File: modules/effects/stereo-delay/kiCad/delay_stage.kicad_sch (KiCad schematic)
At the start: 23 parts, among them Q2 2N3904, U6 PT2399

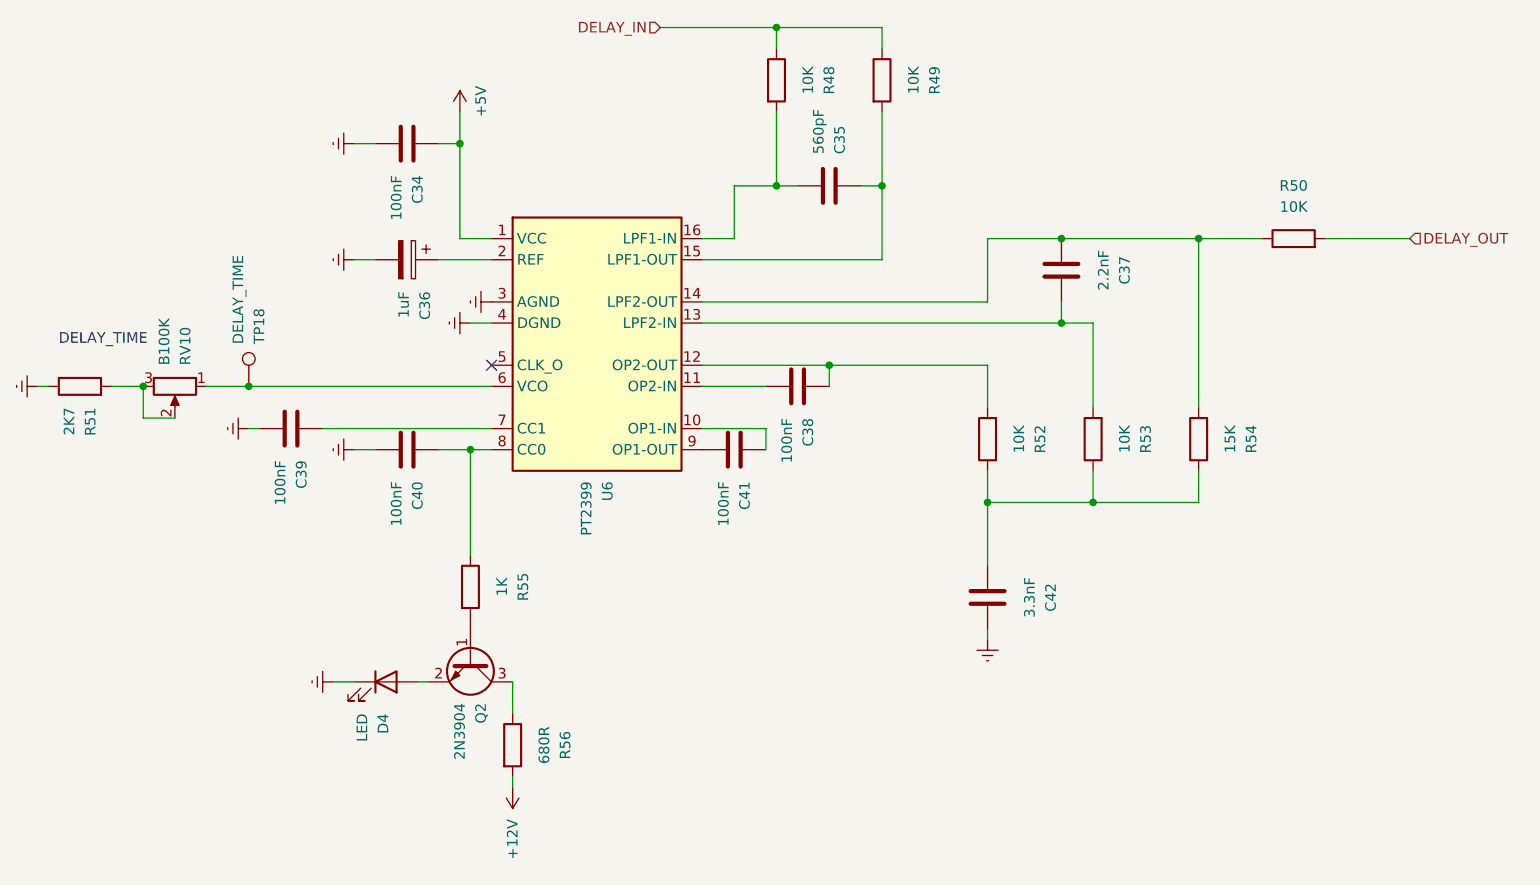
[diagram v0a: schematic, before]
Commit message: Add: Quantizer init, Fix: Stereo-Delay, Fix: Midi-2-xc
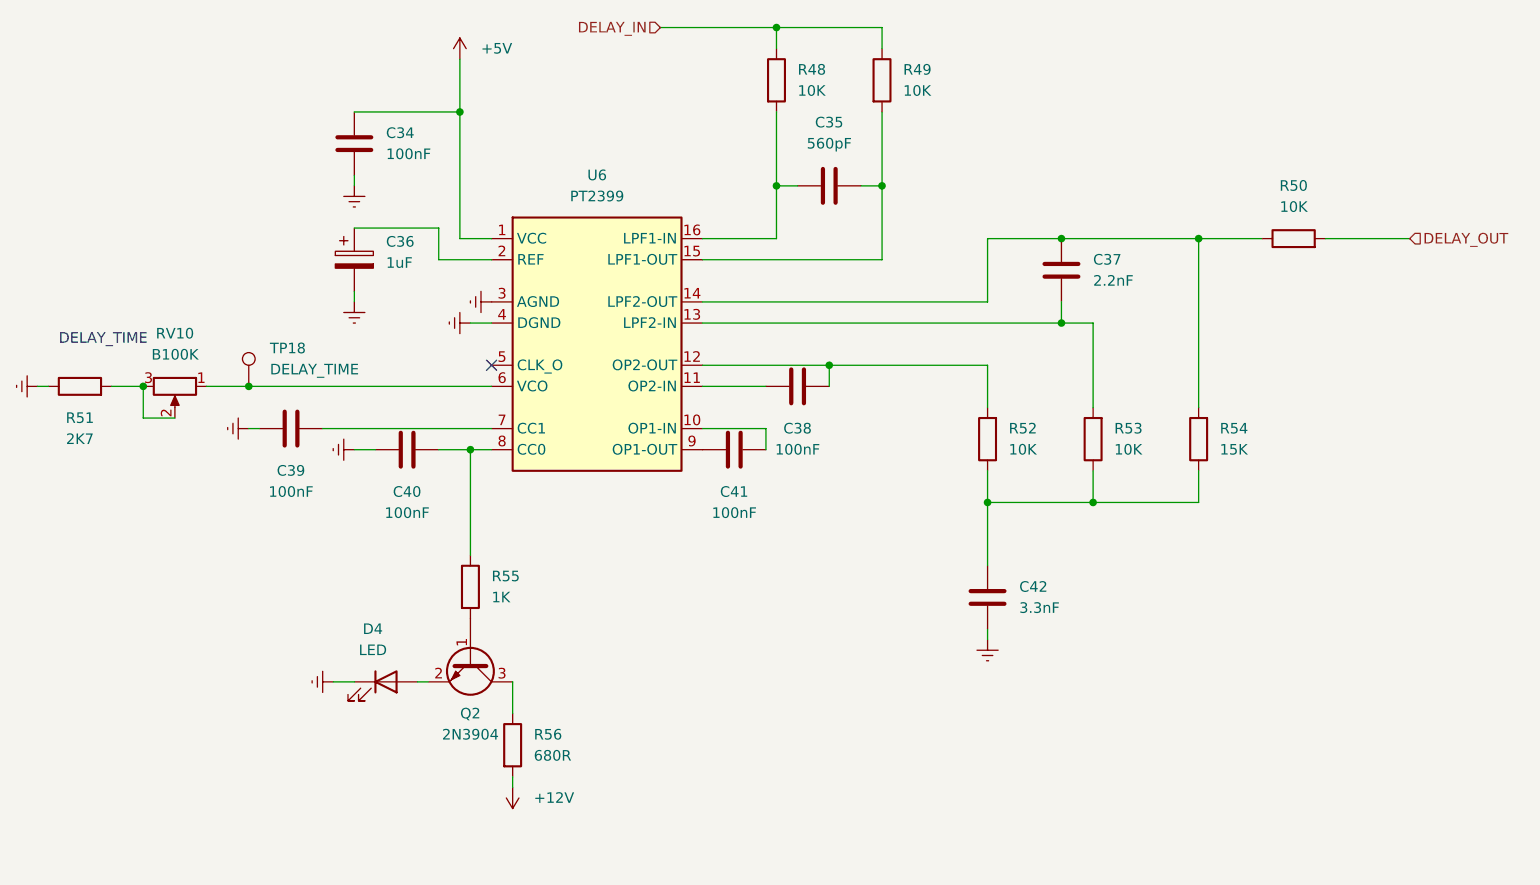
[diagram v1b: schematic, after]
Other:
- moved on the sheet: C34, C36
